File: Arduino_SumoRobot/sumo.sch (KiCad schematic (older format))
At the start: 43 parts, among them IC1 40106D, J1 HEADER_4, K1 RELAY_C, K2 RELAY_C, K3 RELAY_C, K4 RELAY_C, P1 Power, P10 CONN_01X04, P11 CONN_01X04, P12 CONN_01X02, P2 Analog, P3 Digital, P4 Digital, P5 CONN_1, P6 CONN_1, P7 CONN_1, P8 CONN_1, P9 CONN_01X06, Q1 S8050, Q2 S8050, Q3 S8050, Q4 S8050, U1 CNY70, U2 CNY70, U3 CNY70, U4 CNY70

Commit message: Reorganizo bibliotecas del Arduino_SumoRobot.
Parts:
- 1K1, R1, R13, R14, R15, R2, R3, R4, R5, R6, R7, R8: footprint Resistors_ThroughHole:Resistor_Horizontal_RM7mm -> huellas:Resistor_Horizontal_RM7mm
- 1n1, 1n2, 1n3, 1n4: footprint Diodes_SMD:SMC_Standard -> huellas:SMC_Standard
- C1: footprint Capacitors_ThroughHole:C_Rect_L7_W6_P5 -> huellas:C_Rect_L7_W6_P5
- IC1: footprint 40xx:40xx-DIL16 -> huellas:40xx-DIL16
- J1: footprint Pin_Headers:Pin_Header_Straight_1x04 -> huellas:Pin_Header_Straight_1x04
- K1, K2, K3, K4: footprint Relays_ThroughHole:Relay_SANYOU_SRD_Series_Form_C -> huellas:Relay_SANYOU_SRD_Series_Form_C
- P1, P4: footprint Socket_Arduino_Uno:Socket_Strip_Arduino_1x08 -> huellas:Socket_Strip_Arduino_1x08
- P10, P11: footprint Pin_Headers:Pin_Header_Straight_1x04_Pitch2.00mm -> huellas:Pin_Header_Straight_1x04_Pitch2.00mm
- P12: footprint Pin_Headers:Pin_Header_Straight_1x02_Pitch2.00mm -> huellas:Pin_Header_Straight_1x02_Pitch2.00mm
- P2: footprint Socket_Arduino_Uno:Socket_Strip_Arduino_1x06 -> huellas:Socket_Strip_Arduino_1x06
- P3: footprint Socket_Arduino_Uno:Socket_Strip_Arduino_1x10 -> huellas:Socket_Strip_Arduino_1x10
- P5, P6, P7, P8: footprint Socket_Arduino_Uno:Arduino_1pin -> huellas:Arduino_1pin
- P9: footprint Pin_Headers:Pin_Header_Straight_1x06 -> huellas:Pin_Header_Straight_1x06
- Q1, Q2, Q3, Q4: footprint TO_SOT_Packages_THT:TO-92_Rugged -> huellas:TO-92_Rugged
- U1, U2, U3, U4: footprint cny70:cny70-4 -> huellas:cny70-4

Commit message: Sugerencias del esquemático del Arduino_sumo.
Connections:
- wire segments 187 -> 183
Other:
- note added: "OJO!"
- moved on the sheet: 1n4, C1, IC1G, K4, Q4

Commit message: Agrego avances y algunas correcciones propias: etiquetas 5V, serigrafía, prolijidad.
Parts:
- removed J1: HEADER_4, huellas:Pin_Header_Straight_1x04, symbol HEADER_4
- removed U1, U2, U3, U4: CNY70, huellas:cny70-4, symbol CNY70
- added LD1, LD2, LD3, LD4, LD5: LED3MM, Led:led-LED3MM, symbol LED3MM
- added P13, P14, P15, P16: CONN_01X04, Pin_Headers:Pin_Header_Straight_1x04, symbol CONN_01X04
- added P17, P18: CONN_01X02, Pin_Headers:Pin_Header_Straight_1x02, symbol CONN_01X02
- added R10, R11, R12, R16, R9: 220, huellas:Resistor_Horizontal_RM7mm, symbol R-RESCUE-Arduino_As_Uno
- 1n1, 1n2, 1n3, 1n4: footprint huellas:SMC_Standard -> Diodes_ThroughHole:Diode_DO-41_SOD81_Horizontal_RM10
- P10, P11: footprint huellas:Pin_Header_Straight_1x04_Pitch2.00mm -> huellas:Pin_Header_Straight_1x04
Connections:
- net labels removed: 12(MISO), 13(SCK), IOREF, Reset, VCC
- wire segments 183 -> 253
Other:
- note removed: "OJO!"
- moved on the sheet: 1n4, K4, P10, P11, P12, Q4

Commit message: Corrijo Dip16 a Dip14, Corrijo net 12V, Limpio placa para rerutear.
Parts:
- IC1: footprint huellas:40xx-DIL16 -> Housings_DIP:DIP-14_W7.62mm_LongPads
- P12: footprint huellas:Pin_Header_Straight_1x02_Pitch2.00mm -> Connect:bornier2
- P17, P18: footprint Pin_Headers:Pin_Header_Straight_1x02 -> Connect:bornier2
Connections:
- wire segments 253 -> 225
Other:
- moved on the sheet: IC1G, P12

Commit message: Correcciones varias, serigrafía, ruteo, borneras, puentes, planos, etc.
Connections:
- net at K4.1: now also P18.1 (P1); no longer P18.2 (P2)
- net at K1.1: now also P18.2 (P2); no longer P18.1 (P1)
- net at K2.1: now also P17.1 (P1); no longer P17.2 (P2)
- net at K3.1: now also P17.2 (P2); no longer P17.1 (P1)
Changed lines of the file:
@@
 F 3 "" H 11000 4875 50  0000 C CNN
 	1    11000 4875
-	1    0    0    -1
+	1    0    0    1
 $EndComp
 $Comp
@@
 F 3 "" H 10975 2000 50  0000 C CNN
 	1    10975 2000
-	1    0    0    -1
+	1    0    0    1
 $EndComp
 $Comp

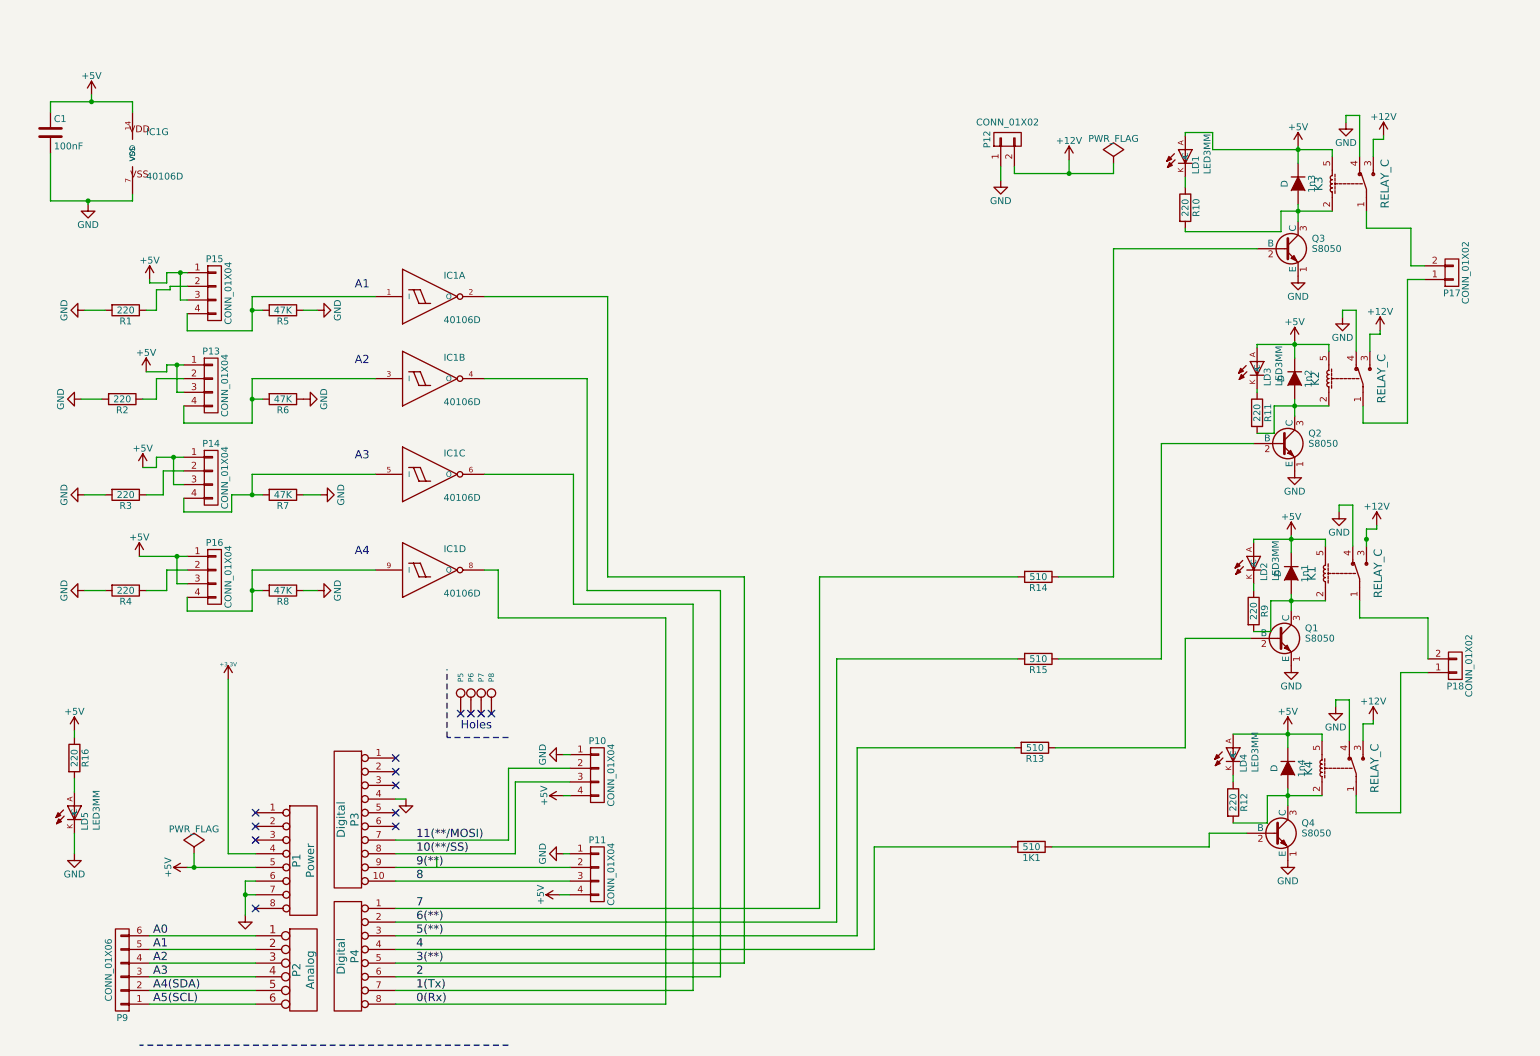
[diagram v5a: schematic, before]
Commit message: Primer borrador de la versión 2 de la placa Arduino Sumo.
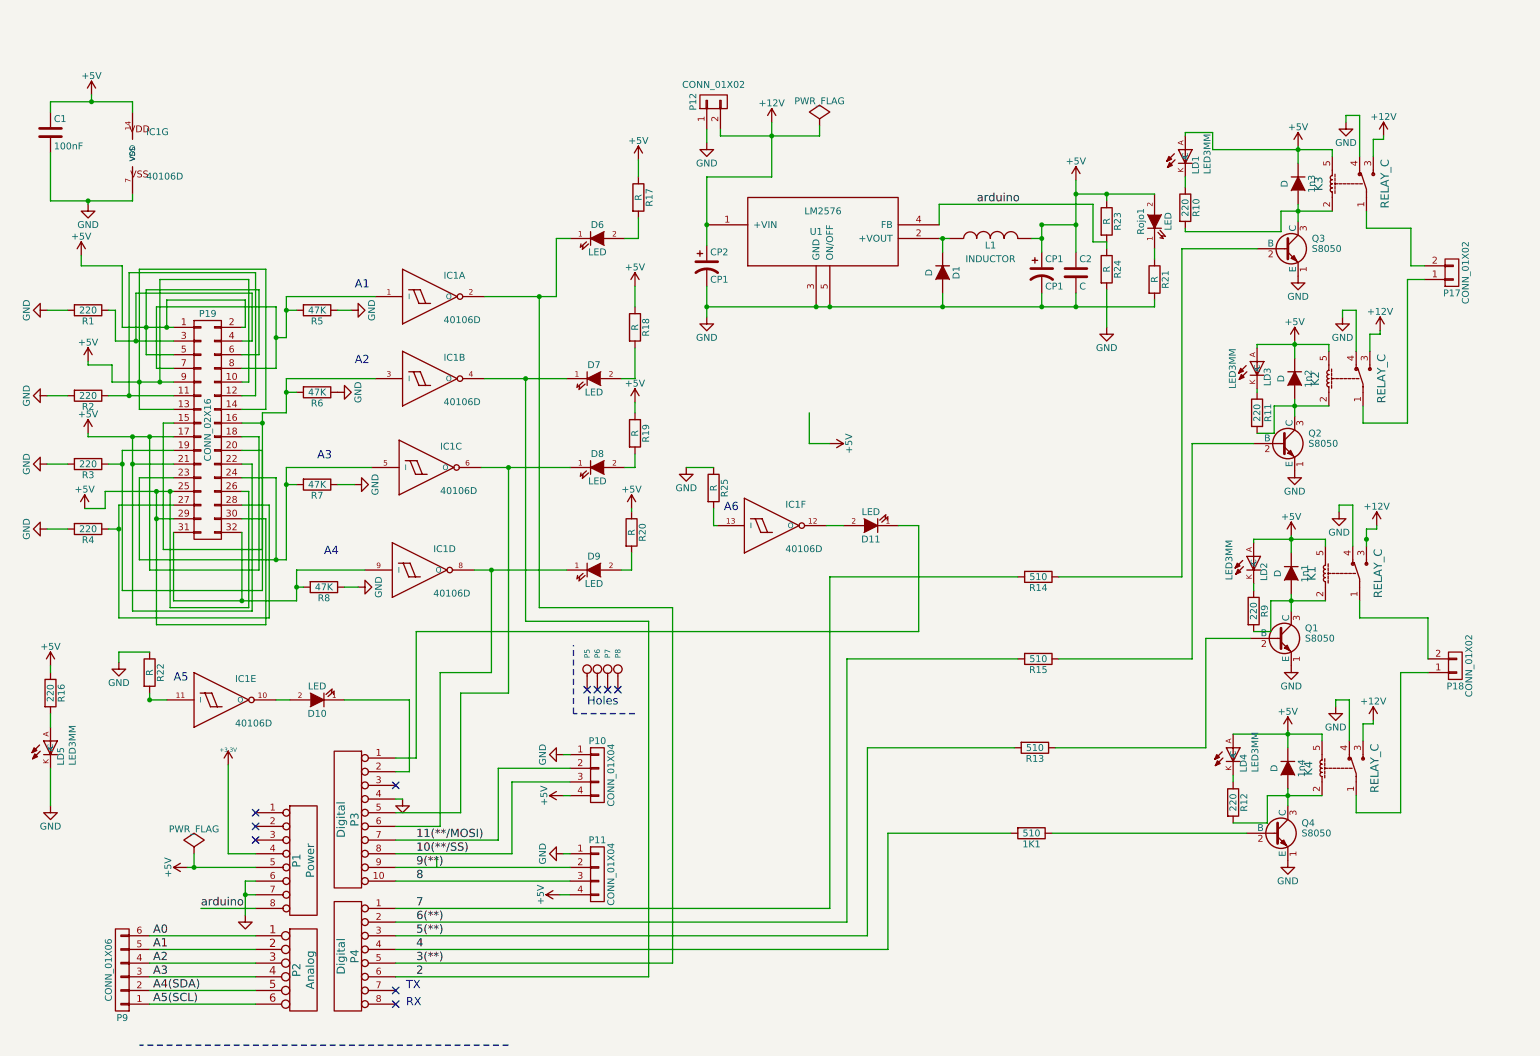
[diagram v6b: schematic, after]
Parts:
- removed P13, P14, P15, P16: CONN_01X04, Pin_Headers:Pin_Header_Straight_1x04, symbol CONN_01X04
- added C2: C, Capacitors_ThroughHole:C_Rect_L7_W6_P5, symbol C
- added CP1, CP2: CP1, Capacitors_ThroughHole:C_Radial_D6.3_L11.2_P2.5, symbol CP1
- added D1: D, Diodes_ThroughHole:Diode_DO-41_SOD81_Horizontal_RM10, symbol D
- added D10, D11, D6, D7, D8, D9, Rojo1: LED, LEDs:LED-5MM, symbol LED
- added unit 6 of IC1
- added unit 5 of IC1
- added L1: INDUCTOR, Inductors:INDUCTOR_V, symbol INDUCTOR
- added P19: CONN_02X16, Pin_Headers:Pin_Header_Straight_2x16_Pitch2.00mm, symbol CONN_02X16
- added R17, R18, R19, R20, R21, R22, R23, R24, R25: R, Resistors_ThroughHole:Resistor_Horizontal_RM7mm, symbol R
- added U1: LM2576, huellas:TO220-51, symbol LM2576
- LD5: footprint Led:led-LED3MM -> led-LED3MM
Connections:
- net +12V: now also CP2.1, U1.1 (+VIN)
- net +5V: now also C2.1, CP1.1, L1.2, P19.1 (P1), P19.10 (P10), P19.13 (P13), P19.14 (P14), P19.17 (P17), P19.18 (P18), P19.2 (P2), P19.21 (P21), P19.22 (P22), P19.25 (P25), P19.26 (P26), P19.29 (P29), P19.30 (P30), P19.5 (P5), P19.6 (P6), P19.9 (P9), R17.1, R18.1, R19.1, R20.1, R23.1, Rojo1.2 (A)
- net 2: now also D7.1 (K)
- net 3(**): now also D6.1 (K)
- net GND: now also C2.2, CP1.2, CP2.2, D1.2 (A), R21.2, R22.1, R24.2, R25.1, U1.3 (GND), U1.5 (ON/OFF)
- net arduino: now reaches P1.8 (P8)
- net arduino: now also R23.2, R24.1, U1.4 (FB)
- net at P3.1 (P1): now also D11.1 (K)
- net at P3.2 (P2): now also D10.1 (K)
- net at P3.5 (P5): now also IC1.6 (O), D8.1 (K)
- net at P3.6 (P6): now also IC1.8 (O), D9.1 (K)
- net at R1.1: now also P19.3 (P3), P19.4 (P4)
- net at R2.1: now also P19.11 (P11), P19.12 (P12)
- net at R3.1: now also IC1.3 (I), R6.2, P19.15 (P15), P19.16 (P16), P19.19 (P19), P19.20 (P20)
- net at R4.1: now also P19.27 (P27), P19.28 (P28)
- net at IC1.1 (I), R5.2: now also P19.7 (P7), P19.8 (P8)
- net at IC1.5 (I), R7.2: now also P19.23 (P23), P19.24 (P24)
- net at IC1.9 (I), R8.2: now also P19.31 (P31), P19.32 (P32)
- net 0(Rx): no longer names the net of P4.8 (P8)
- net 0(Rx): no longer IC1.8 (O)
- net 1(Tx): no longer names the net of P4.7 (P7)
- net 1(Tx): no longer IC1.6 (O)
- new net: D7.2 (A), R18.2
- new net: D8.2 (A), R19.2
- new net: D9.2 (A), R20.2
- new net: D6.2 (A), R17.2
- new net: D1.1 (K), L1.1, U1.2 (+VOUT)
- new net: R21.1, Rojo1.1 (K)
- new net: IC1.13 (I), R25.2
- new net: D11.2 (A), IC1.12 (O)
- new net: IC1.11 (I), R22.2
- new net: D10.2 (A), IC1.10 (O)
- no-connect marks 13 -> 10
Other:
- note added: "A5\n"
- note added: "A6\n\n"
- note added: "RX\n"
- note added: "TX"
- moved on the sheet: 1K1, IC1C, IC1D, P12, P5, P6, P7, P8, R1, R16, R2, R3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

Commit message: Cambios en el esquemático y asignación de huellas dentro del proyecto.
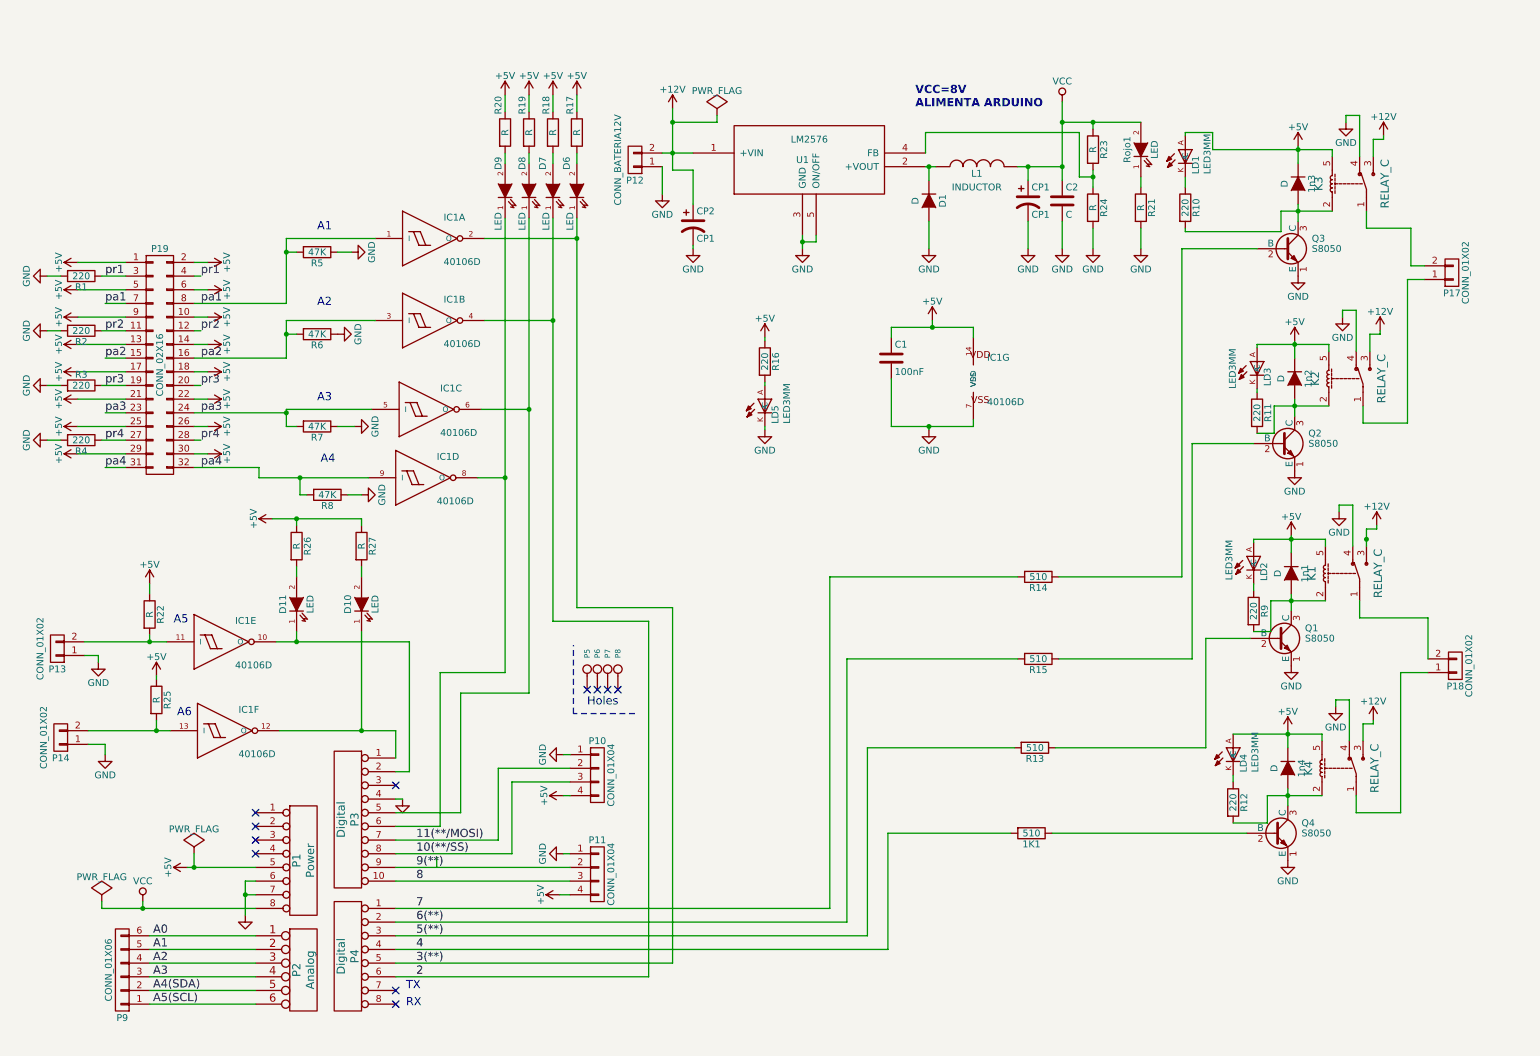
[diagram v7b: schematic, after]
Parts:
- added P13, P14: CONN_01X02, huellas:bornier2, symbol CONN_01X02
- added R26, R27: R, huellas:Resistor_Horizontal_RM7mm, symbol R
- 1n1, 1n2, 1n3, 1n4, D1: footprint Diodes_ThroughHole:Diode_DO-41_SOD81_Horizontal_RM10 -> huellas:Diode_DO-41_SOD81_Horizontal_RM10
- C2: footprint Capacitors_ThroughHole:C_Rect_L7_W6_P5 -> huellas:C_Rect_L7_W6_P5
- CP1, CP2: footprint Capacitors_ThroughHole:C_Radial_D6.3_L11.2_P2.5 -> huellas:C_Radial_D6.3_L11.2_P2.5
- D10, D11, D6, D7, D8, D9, Rojo1: footprint LEDs:LED-5MM -> huellas:LED-5MM
- IC1: footprint Housings_DIP:DIP-14_W7.62mm_LongPads -> huellas:DIP-14_W7.62mm_LongPads
- L1: footprint Inductors:INDUCTOR_V -> huellas:INDUCTOR_V
- LD1, LD2, LD3, LD4: footprint Led:led-LED3MM -> huellas:led-LED3MM
- LD5: footprint led-LED3MM -> huellas:led-LED3MM
- P12: value CONN_01X02 -> CONN_BATERIA12V; footprint Connect:bornier2 -> huellas:bornier2
- P17, P18: footprint Connect:bornier2 -> huellas:bornier2
- P19: footprint Pin_Headers:Pin_Header_Straight_2x16_Pitch2.00mm -> huellas:Pin_Header_Straight_2x16_Pitch2.00mm
- R17, R18, R19, R20, R21, R22, R23, R24, R25: footprint Resistors_ThroughHole:Resistor_Horizontal_RM7mm -> huellas:Resistor_Horizontal_RM7mm
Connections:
- net +5V: now also R22.1, R25.1, R26.1, R27.1; no longer C2.1, CP1.1, L1.2, R23.1, Rojo1.2 (A)
- net GND: now also P13.1 (P1), P14.1 (P1); no longer R22.1, R25.1
- net at P3.1 (P1): now also D10.1 (K), IC1.12 (O); no longer D11.1 (K)
- net at P3.2 (P2): now also D11.1 (K), IC1.10 (O); no longer D10.1 (K)
- net pr1: now reaches P19.3 (P3), P19.4 (P4), R1.1
- net pr2: now reaches P19.11 (P11), P19.12 (P12), R2.1
- net pa2: now reaches IC1.3 (I), P19.15 (P15), P19.16 (P16), R6.2
- net pa2: no longer P19.19 (P19), P19.20 (P20), R3.1
- net pr4: now reaches P19.27 (P27), P19.28 (P28), R4.1
- net pa1: now reaches IC1.1 (I), P19.7 (P7), P19.8 (P8), R5.2
- net pa3: now reaches IC1.5 (I), P19.23 (P23), P19.24 (P24), R7.2
- net pa4: now reaches IC1.9 (I), P19.31 (P31), P19.32 (P32), R8.2
- net at IC1.13 (I), R25.2: now also P14.2 (P2)
- net at D11.2 (A): now also R26.2; no longer IC1.12 (O)
- net at IC1.11 (I), R22.2: now also P13.2 (P2)
- net at D10.2 (A): now also R27.2; no longer IC1.10 (O)
- net arduino: no longer names the net of R23.2, R24.1, U1.4 (FB)
- net arduino: no longer P1.8 (P8)
- new net VCC: C2.1, CP1.1, L1.2, P1.8 (P8), R23.1, Rojo1.2 (A)
- new net pr3: P19.19 (P19), P19.20 (P20), R3.1
- no-connect marks 10 -> 11
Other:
- note added: "VCC=8V\nALIMENTA ARDUINO"
- moved on the sheet: C1, C2, CP1, CP2, D1, D10, D11, D6, D7, D8, D9, IC1A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
